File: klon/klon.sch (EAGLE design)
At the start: 8 parts, among them IC1 TL072P

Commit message: library tweaks.
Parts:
- added U$1: (no value), perfboards:GREEN-2-SIDED9X7
- added U$2: 2_1MM-JACK-PLUG, pedal-lilbrary:2_1MM-JACK-PLUG
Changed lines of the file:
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@@
 <part name="C2" library="mb-capacitors-film" deviceset="CER/FILM" device="3" value="0.1uF"/>
 <part name="C3" library="mb-capacitors-film" deviceset="CER/FILM" device="3" value="0.1uF"/>
+<part name="U$1" library="perfboards" deviceset="GREEN-2-SIDED" device="9X7"/>
+<part name="U$2" library="pedal-lilbrary" deviceset="2_1MM-JACK-PLUG" device=""/>
 </parts>
 <sheets>
@@
 <attribute name="VALUE" x="94.234" y="121.158" size="1.778" layer="96" rot="R180"/>
 </instance>
+<instance part="U$1" gate="G$1" x="10.16" y="154.94" smashed="yes">
+<attribute name="SIDES" x="18.034" y="155.702" size="1.016" layer="95"/>
+<attribute name="WIDTH" x="17.78" y="163.068" size="1.016" layer="95" align="bottom-center"/>
+<attribute name="HEIGHT" x="26.924" y="158.75" size="1.016" layer="95" rot="R90" align="bottom-center"/>
+</instance>
+<instance part="U$2" gate="G$1" x="20.32" y="137.16" smashed="yes">
+<attribute name="NAME" x="12.7" y="142.24" size="1.778" layer="95"/>
+<attribute name="VALUE" x="12.7" y="132.08" size="1.778" layer="96"/>
+</instance>
 </instances>

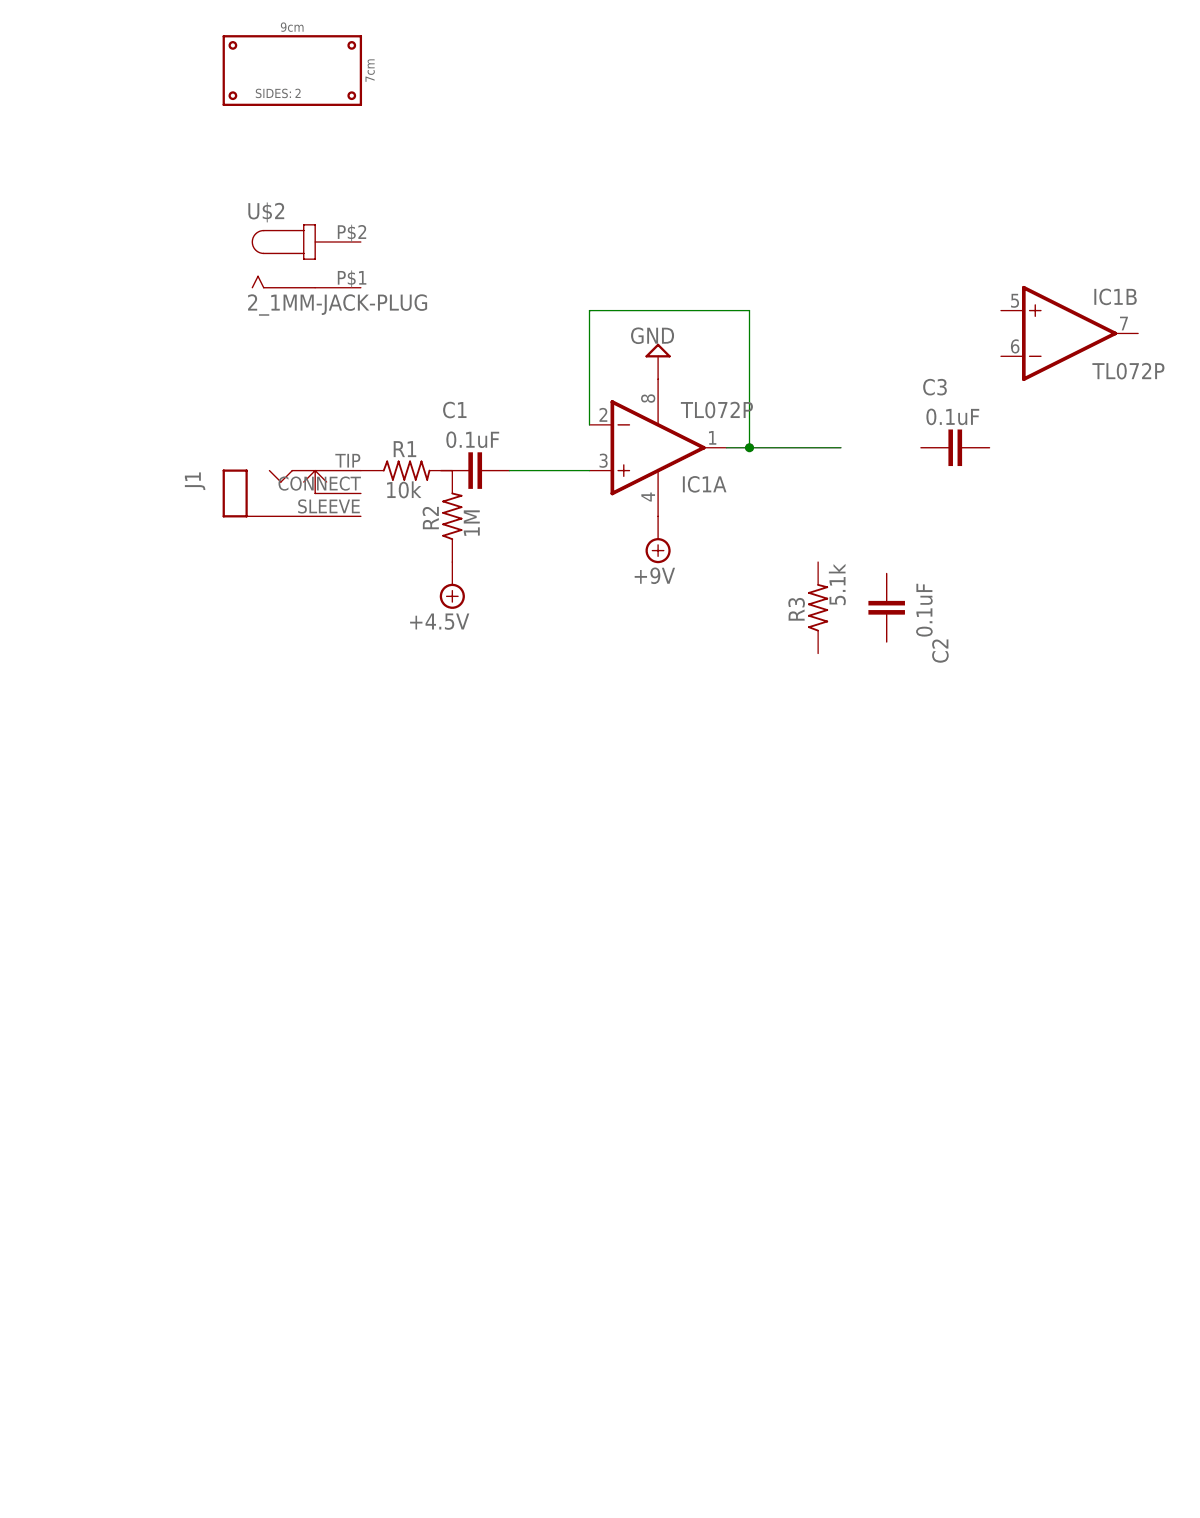
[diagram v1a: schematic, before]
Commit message: Add klon power.
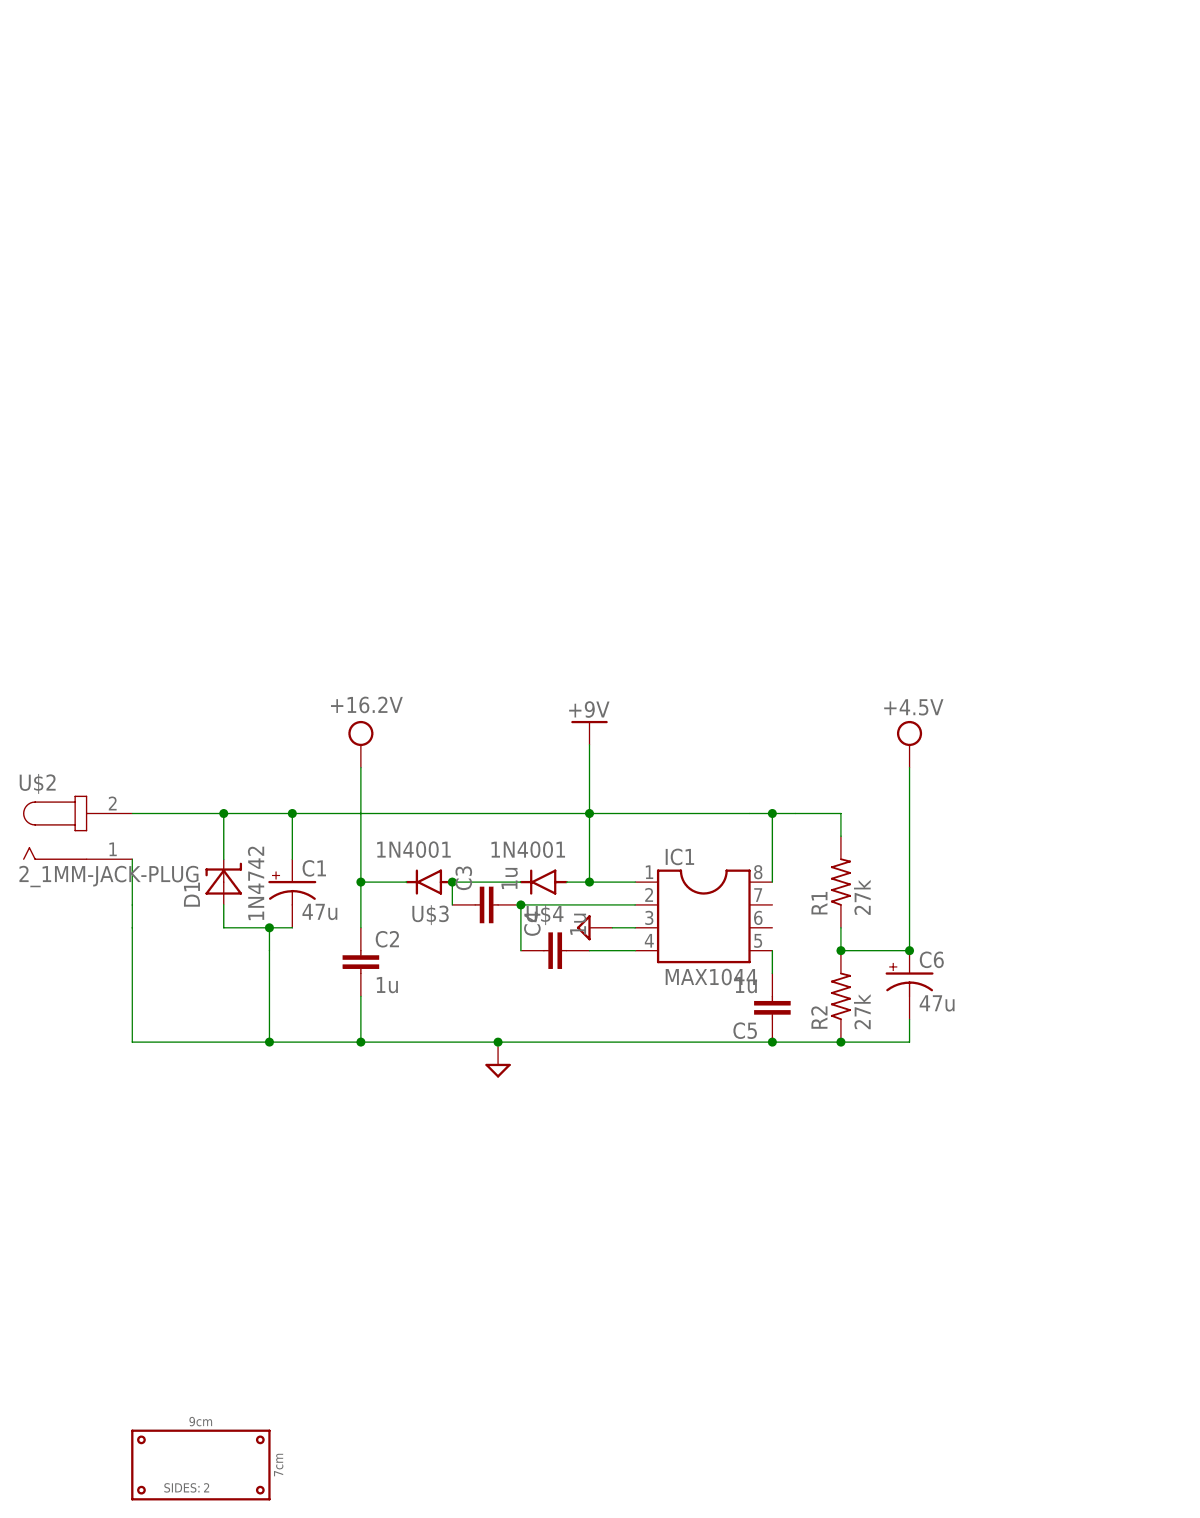
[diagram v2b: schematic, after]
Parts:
- removed J1: (no value), mb-jacks:CLOSEDMONO
- removed R3: 5.1k, mb-resistors:R_.4
- added C4, C5: 1u, pedal-library:C-MM025-025X050
- added C6: 47u, pedal-library:C-E0.1_0.15
- added D1: 1N4742, pedal-library:1N4742
- added U$3, U$4: 1N4001, pedal-library:1N4001
- C1: value 0.1uF -> 47u; device mb-capacitors-film:CER/FILM3 -> pedal-library:C-E0.1_0.15
- C2, C3: value 0.1uF -> 1u; device mb-capacitors-film:CER/FILM3 -> pedal-library:C-MM025-025X050
- IC1: value TL072P -> MAX1044; device linear:TL072P -> MAX1044:MAX1044
- R1: value 10k -> 27k; device mb-resistors:R_.4 -> pedal-library:RESISTOR0204/7
- R2: value 1M -> 27k; device mb-resistors:R_.4 -> pedal-library:RESISTOR0204/7
- U$2: device pedal-lilbrary:2_1MM-JACK-PLUG -> pedal-library:2_1MM-JACK-PLUG
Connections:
- removed net +5V: R2.1
- removed net N$1: J1.TIP, R1.1
- removed net N$4: IC1A.-IN, IC1A.OUT
- new net +16.2V: C2.1, U$3.C
- new net +4.5V: C6.+, R1.1, R2.2
- new net N$5: C4.2, IC1.4
- new net N$6: C3.2, C4.1, IC1.2
- net +9V: now also C1.+, D1.C, IC1.1, IC1.8, R1.2, U$2.GND, U$4.A; no longer IC1P.V-
- net GND: now also C1.-, C2.2, C5.1, C6.-, D1.A, IC1.3, R2.1, U$2.+9V; no longer IC1P.V+
- net N$2: now also C5.2, IC1.5; no longer R1.2, R2.2
- net N$3: now also C3.1, U$3.A, U$4.C; no longer C1.2, IC1A.+IN
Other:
- moved on the sheet: R1, R2, U$2

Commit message: Klon schematic
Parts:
- added C10, C9: 68n, capacitor-wima:C10/5
- added C11, C13, C18: 1µ, pedal-library:C-E0.1_0.15
- added C12: 390p, pedal-library:C-CERAMICC-C-0.1_0.05
- added C14: 82n, pedal-library:C-PP_0.60.2W
- added C15: 2.2n, pedal-library:C-PP_0.40.15
- added C16: 22n, pedal-library:C-PP_0.40.2
- added C17: 4.7n, pedal-library:C-PP_0.40.2
- added C19: 470p, pedal-library:C-CERAMICC-C-0.1_0.05
- added C20: 330p, pedal-library:C-CERAMICC-C-0.1_0.05
- added C21: 3.9n, pedal-library:C-PP_0.40.1
- added C22: 4.7, pedal-library:C-E0.1_0.15
- added C7, C8: 0.1µ, capacitor-wima:C10/5
- added D2, D3: 1N34A, diode:DIODE-D-7.5
- added IC2, IC3: TL072P, linear:TL072P
- added LEVEL, TREBLE: 10kB, pedal-library:POT-1X
- added R10, R18: 15k, pedal-library:RESISTOR0204/7
- added R11: 422k, pedal-library:RESISTOR0204/7
- added R12, R8: 1k, pedal-library:RESISTOR0204/7
- added R13: 47k, pedal-library:RESISTOR0204/7
- added R14: 22k, pedal-library:RESISTOR0204/7
- added R15: 27k, pedal-library:RESISTOR0204/7
- added R16: 12k, pedal-library:RESISTOR0204/7
- added R17, R7: 1.5k, pedal-library:RESISTOR0204/7
- added R19: 392K, pedal-library:RESISTOR0204/7
- added R20, R22: 100k, pedal-library:RESISTOR0204/7
- added R21: 1.8k, pedal-library:RESISTOR0204/7
- added R23: 4.7k, pedal-library:RESISTOR0204/7
- added R24: 560, pedal-library:RESISTOR0204/7
- added R25, R26: 68K, pedal-library:RESISTOR0204/7
- added R3, R5: 10k, pedal-library:RESISTOR0204/7
- added R4: 1M, pedal-library:RESISTOR0204/7
- added R6: 5.1k, pedal-library:RESISTOR0204/7
- added R9: 2k, pedal-library:RESISTOR0204/7
- added RV-GAIN: 100k, pedal-library:POT-2X
- added S1: 3PDT9-PIN-HEADER, pedal-library:3PDT9-PIN-HEADER
- added U$5: INSTRUMENT-JACKPINS, pedal-library:INSTRUMENT-JACKPINS
- added U$7: 330n, pedal-library:C-PP_0.60.15W
- C1: value 47u -> 47µ
- C2, C3, C4, C5: value 1u -> 1µ; device pedal-library:C-MM025-025X050 -> pedal-library:C-E0.1_0.15
- U$1: value (none) -> 9x7
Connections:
- new net -8.6V: C4.+, IC1.5, IC3P.V-
- new net N$1: C2.-, C3.+, IC1.2
- new net N$10: C10.2, C8.1, IC2A.-IN, IC2A.OUT, R6.2
- new net N$11: C10.1, R6.1, R7.2, RV-GAINB.E, U$7.2
- new net N$12: R9.2, RV-GAINA.A
- new net N$13: C14.1, R10.2, R9.1
- new net N$14: C11.-, R12.1
- new net N$15: C13.-, D2.C, D3.A, R12.2
- new net N$16: C11.+, C12.1, IC2B.OUT, R11.1
- new net N$17: C12.2, C14.2, IC2B.-IN, R10.1, R11.2
- new net N$18: C13.+, C15.2, R13.1
- new net N$19: C15.1, R14.2
- new net N$20: R14.1, R15.1, R16.1, RV-GAINB.S
- new net N$21: C16.1, C17.1, R16.2
- new net N$22: C16.2, C17.2, R15.2, R18.1
- new net N$23: C18.+, R17.1, R18.2
- new net N$24: R21.2, TREBLE.1
- new net N$25: C19.2, C20.2, IC3A.OUT, R19.2, R20.2, R21.1
- new net N$26: C19.1, C20.1, IC3A.-IN, R13.2, R19.1
- new net N$27: C21.1, IC3B.-IN, R20.1, TREBLE.2
- new net N$28: C22.+, IC3B.OUT, R22.1, R23.1
- new net N$29: R23.2, TREBLE.3
- new net N$30: C21.2, R22.2
- new net N$31: C22.-, R24.2
- new net N$32: LEVEL.3, R24.1
- new net N$33: LEVEL.2, R26.1, S1.O3
- new net N$34: R25.1, S1.S3
- new net N$35: R25.2, R26.2, S1.P3
- new net N$4: C2.+, U$3.A, U$4.C
- new net N$7: R8.2, U$7.1
- new net N$8: C8.2, C9.1, R17.2, R5.1
- new net N$9: C9.2, IC2B.+IN, R5.2, RV-GAINA.E
- net +16.2V: now also C5.+, IC3P.V+; no longer C2.1
- net +4.5V: now also IC3A.+IN, IC3B.+IN, R7.1, R8.1, RV-GAINA.S, RV-GAINB.A
- net +9V: now also IC2P.V+, U$2.+9V; no longer U$2.GND
- net GND: now also C18.-, C4.-, C5.-, D2.A, D3.C, IC2P.V-, LEVEL.1, R4.1, U$2.GND, U$5.S; no longer C2.2, C5.1, U$2.+9V
- net N$2: now also C3.-, IC1.4; no longer C5.2, IC1.5
- net N$3: now also C7.1, R3.2; no longer C3.1, U$3.A, U$4.C
- net N$5: now also R3.1, U$5.T; no longer C4.2, IC1.4
- net N$6: now also C7.2, IC2A.+IN, R4.2; no longer C3.2, C4.1, IC1.2
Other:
- moved on the sheet: C1, C6, D1, IC1, R1, R2
